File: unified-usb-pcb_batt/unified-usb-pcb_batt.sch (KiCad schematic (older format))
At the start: 39 parts, among them J1 QI, J2 USB_C_Receptacle_USB2.0, J3 USB_Out, J4 BATT, J5 THERM, SW1 SW_SPDT, U1 SRV05-4, U2 DW01A, U3 TP4056, U4 FS8205

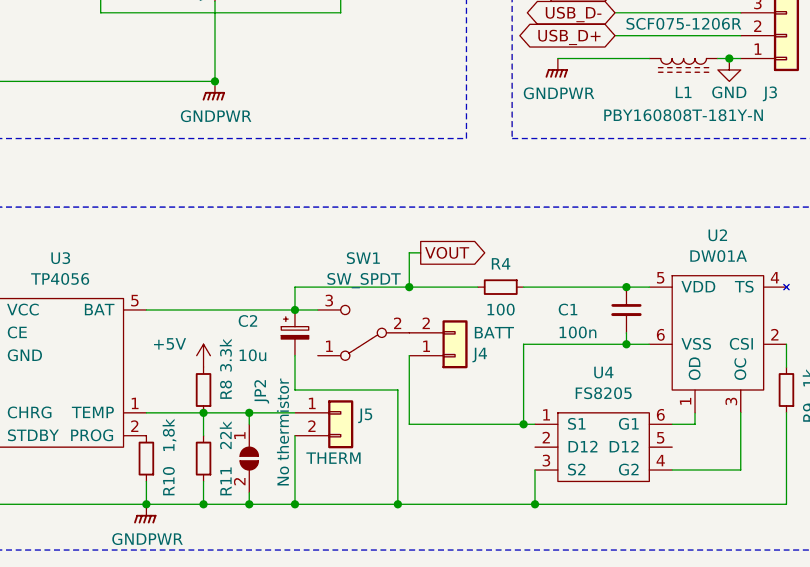
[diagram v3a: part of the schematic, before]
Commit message: fixed batt schem, added readme warning about broken pcb
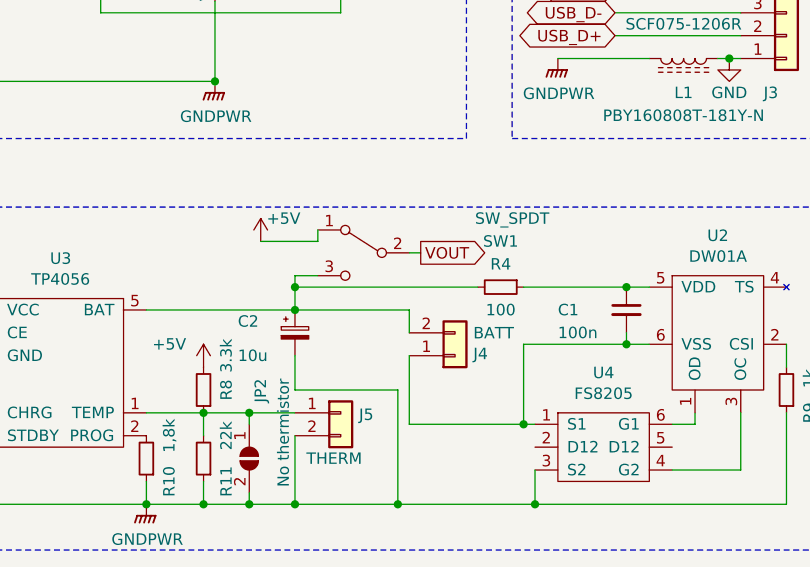
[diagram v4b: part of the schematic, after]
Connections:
- net +5V: now also SW1.1 (A)
- net VOUT: now also SW1.2 (B); no longer C2.1, R4.2, SW1.3 (C), U3.5 (BAT)
- net at J4.2 (Pin_2): now also C2.1, R4.2, SW1.3 (C), U3.5 (BAT); no longer SW1.2 (B)
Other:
- moved on the sheet: SW1
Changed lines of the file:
@@
 	4200 3500 4650 3500
 Connection ~ 4650 3500
-Wire Wire Line
-	3700 3350 3700 3500
-Wire Wire Line
-	4000 3500 3700 3500
 Wire Notes Line style solid
 	550  700  550  2850
@@
 Wire Wire Line
 	1800 3800 1800 4000
-Connection ~ 3700 3500
 Wire Wire Line
 	3000 4400 3000 4450
@@
 	1    0    0    -1
 $EndComp
-$Comp
-L Switch:SW_SPDT SW1
-U 1 1 5E8F7463
-P 3500 3700
-F 0 "SW1" H 3500 3375 50  0000 C CNN
-F 1 "SW_SPDT" H 3500 3466 50  0000 C CNN
-F 2 "kicad-keyboard-parts:ESP3020" H 3500 3700 50  0001 C CNN
-F 3 "https://www.ece.com.tw/images/cgcustom/file020190722095856.pdf" H 3500 3700 50  0001 C CNN
-F 4 "/" H 3500 3700 50  0001 C CNN "LCSC"
-	1    3500 3700
-	-1   0    0    1
-$EndComp
 Wire Wire Line
 	4200 3750 4200 4100
@@
 	3200 3950 3200 3800
 Wire Wire Line
-	3200 3600 3300 3600
-Wire Wire Line
 	3200 3950 3650 3950
 Wire Wire Line
 	3200 3500 3200 3600
-Wire Wire Line
-	3200 3500 3700 3500
 $Comp
 L Mechanical:MountingHole_Pad H1
@@
 Wire Wire Line
 	5100 2500 5050 2500
+$Comp
+L Switch:SW_SPDT SW1
+U 1 1 5E8F7463
+P 3500 3350
+F 0 "SW1" H 2900 3400 50  0000 C CNN
+F 1 "SW_SPDT" H 2850 3500 50  0000 C CNN
+F 2 "kicad-keyboard-parts:ESP3020" H 3500 3350 50  0001 C CNN
+F 3 "https://www.ece.com.tw/images/cgcustom/file020190722095856.pdf" H 3500 3350 50  0001 C CNN
+F 4 "/" H 3500 3350 50  0001 C CNN "LCSC"
+	1    3500 3350
+	-1   0    0    -1
+$EndComp
+Wire Wire Line
+	3200 3500 4000 3500
+Wire Wire Line
+	3700 3600 3700 3700
+Wire Wire Line
+	3200 3600 3700 3600
+Wire Wire Line
+	3300 3450 3200 3450
+Wire Wire Line
+	3200 3450 3200 3500
+Connection ~ 3200 3500
+$Comp
+L power:+5V #PWR?
+U 1 1 5F5849B8
+P 3050 3300
+F 0 "#PWR?" H 3050 3150 50  0001 C CNN
+F 1 "+5V" H 3150 3400 50  0000 C CNN
+F 2 "" H 3050 3300 50  0001 C CNN
+F 3 "" H 3050 3300 50  0001 C CNN
+	1    3050 3300
+	1    0    0    -1
+$EndComp
+Wire Wire Line
+	3050 3300 3300 3300
+Wire Wire Line
+	3300 3300 3300 3250
 $EndSCHEMATC

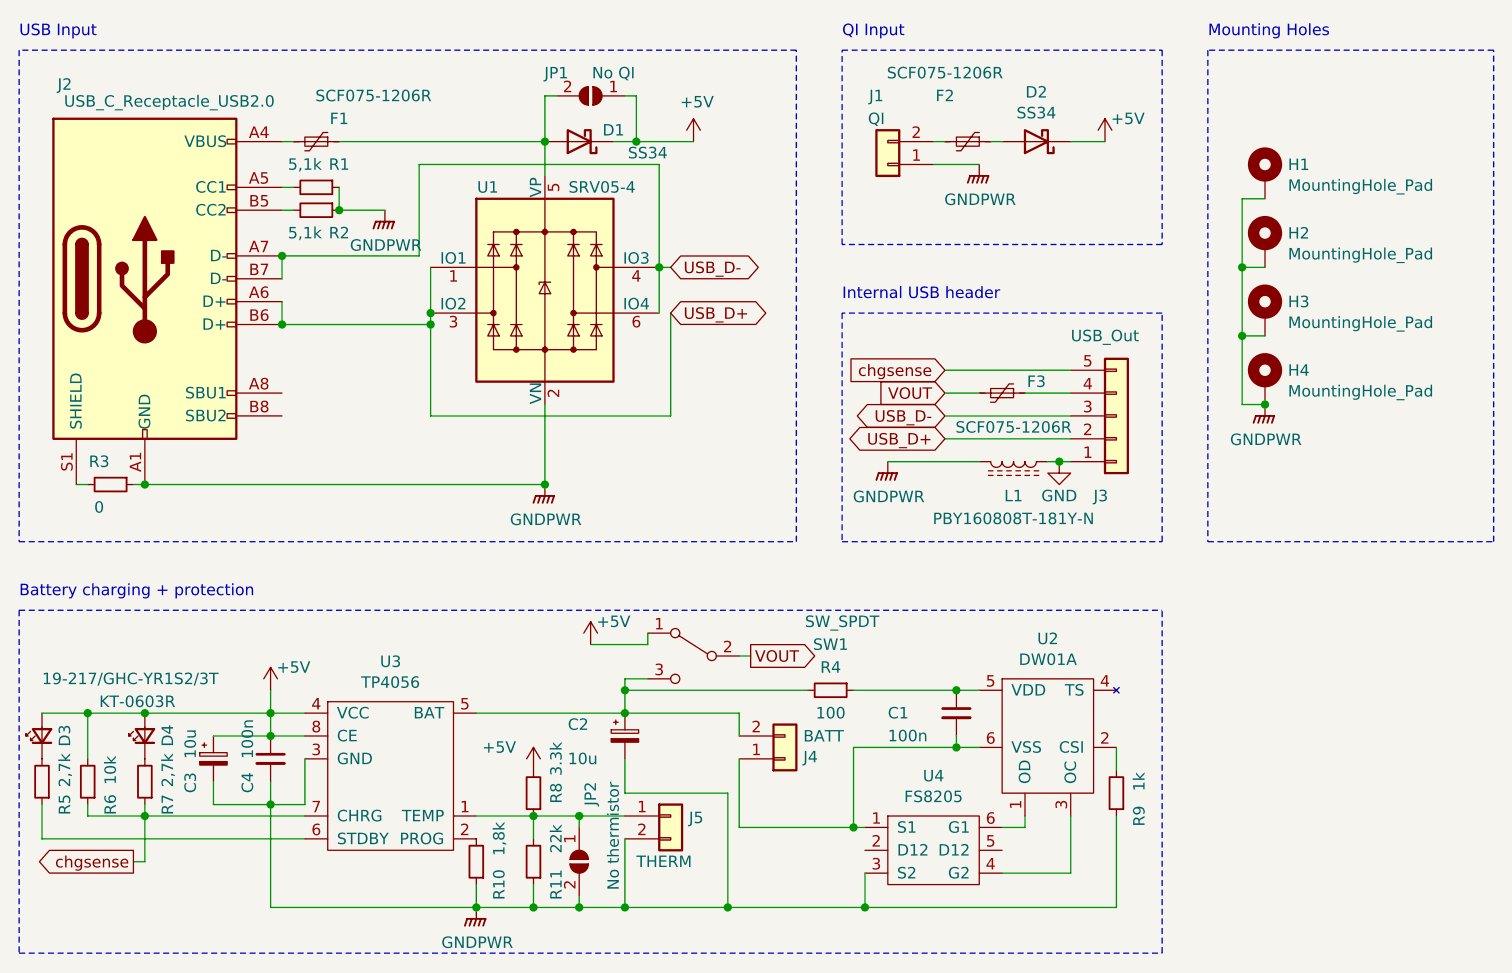
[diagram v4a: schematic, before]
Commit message: removed chargesense, added VBUS detection to schematic
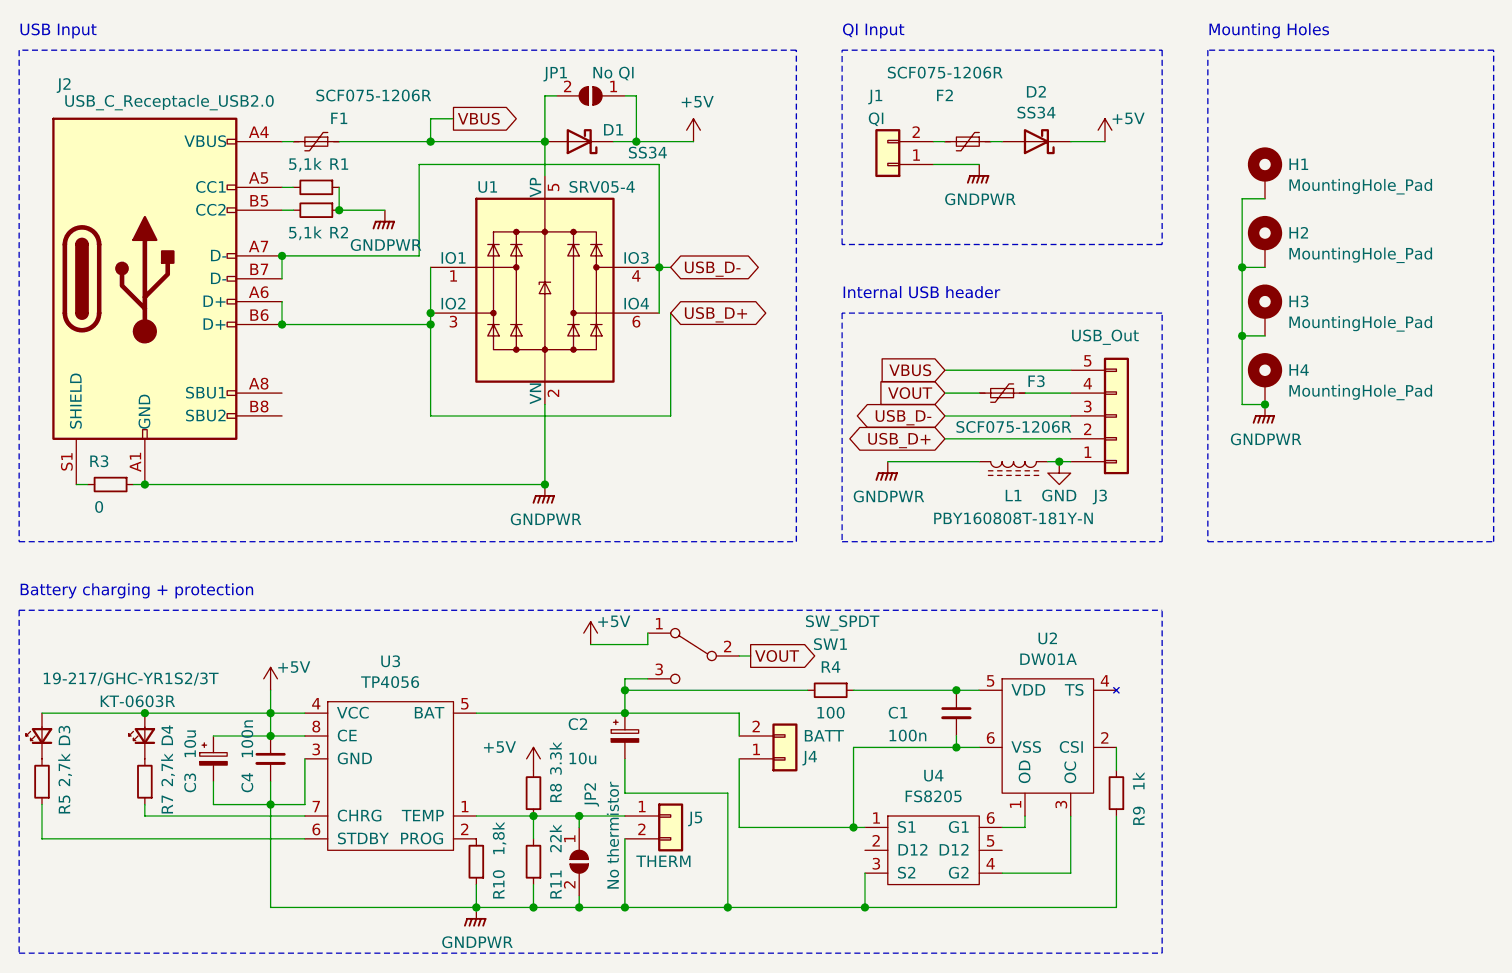
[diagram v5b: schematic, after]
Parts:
- removed R6: 10k, Resistor_SMD:R_0603_1608Metric, symbol Device:R_Small
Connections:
- net VBUS: now reaches D1.2 (A), F1.1, JP1.2 (B), U1.5 (VP)
- net VBUS: now also J3.5 (Pin_5)
- net chgsense: no longer names the net of R7.1, U3.7 (CHRG)
- net chgsense: no longer J3.5 (Pin_5)
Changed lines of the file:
@@
 	2850 1100 2850 1250
 Wire Wire Line
-	1950 1100 2850 1100
+	1950 1100 2350 1100
 $Comp
 L power:GNDPWR #PWR06
@@
 	1    0    0    -1
 $EndComp
-Text GLabel 4600 2100 0    50   Input ~ 0
-chgsense
 Wire Wire Line
 	4600 2100 5150 2100
-$Comp
-L Device:R_Small R6
-U 1 1 5E89839E
-P 850 3900
-F 0 "R6" V 750 4000 50  0000 C CNN
-F 1 "10k" V 750 3850 50  0000 C CNN
-F 2 "Resistor_SMD:R_0603_1608Metric" H 850 3900 50  0001 C CNN
-F 3 "~" H 850 3900 50  0001 C CNN
-F 4 "C25804" H 850 3900 50  0001 C CNN "LCSC"
-	1    850  3900
-	-1   0    0    1
-$EndComp
-Wire Wire Line
-	850  4000 850  4050
-Wire Wire Line
-	850  4050 1100 4050
-Connection ~ 1100 4050
-Wire Wire Line
-	850  3800 850  3600
-Wire Wire Line
-	850  3600 1100 3600
 Wire Wire Line
 	650  4150 1800 4150
-Wire Wire Line
-	850  3600 650  3600
-Connection ~ 850  3600
-Text GLabel 1050 4250 0    50   Output ~ 0
-chgsense
-Wire Wire Line
-	1050 4250 1100 4250
-Wire Wire Line
-	1100 4250 1100 4050
 Wire Notes Line style solid
 	550  3150 5550 3150
@@
 Wire Wire Line
 	3300 3300 3300 3250
+Wire Wire Line
+	650  3600 1100 3600
+Text GLabel 2450 1000 2    50   Output ~ 0
+VBUS
+Wire Wire Line
+	2450 1000 2350 1000
+Wire Wire Line
+	2350 1000 2350 1100
+Connection ~ 2350 1100
+Wire Wire Line
+	2350 1100 2850 1100
+Text GLabel 4600 2100 0    50   Input ~ 0
+VBUS
 $EndSCHEMATC
